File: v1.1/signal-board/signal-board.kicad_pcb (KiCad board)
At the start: 2 copper layers, 32 parts, among them SW1 SW_MEC_5G, SW2 SW_MEC_5G, U1 TPS63060, U2 ESP32-DEVKITC-32D

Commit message: footprint updates
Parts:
- added D1: Red LED, LED_THT:LED_D1.8mm_W3.3mm_H2.4mm, F.Cu at (256.4, 315.7)
- added D2: Green LED, LED_THT:LED_D1.8mm_W3.3mm_H2.4mm, F.Cu at (256.4, 321.4)
- added IC1: 74HCT245, 74HCT245:SOIC-20W_7.5x10.0mm_P1.27mm, F.Cu at (334.8, 248.2)
- added J1: Jack-DC, Connector_BarrelJack:BarrelJack_CUI_PJ-063AH_Horizontal, F.Cu at (322.4, 298.4)
- added J2: Conn_01x12, Connector_PinHeader_2.54mm:PinHeader_1x12_P2.54mm_Vertical, F.Cu at (300.8, 272.6)
- added J3: JST SM, jst-landing-pads:jst-smd-landing, F.Cu at (257.1, 296.4)
- added J4: Conn_01x16, Connector_PinHeader_2.54mm:PinHeader_1x16_P2.54mm_Vertical, F.Cu at (274.6, 335.6)
- SW1, SW2: footprint PTS525SM15SMTR2LFS:SW_PTS525SM15SMTR2LFS -> PTS 647:PTS647SK38SMTR2LFS
- moved U2 136.6 mm to (289.9, 297.4), turned to 90 degrees
- moved SW2 136.4 mm to (273.1, 272.9)
- moved L1 111.8 mm to (311.8, 248.0)
- moved U1 110.7 mm to (296.6, 247.2)
- moved R5 104.8 mm to (264.7, 245.3)
- moved C9 84.7 mm to (266.4, 205.4)
- moved R16 84.7 mm to (261.6, 205.4)
- moved C1 84.7 mm to (248.7, 222.8)
- moved C10 84.7 mm to (243.9, 226.8)
- moved C2 84.7 mm to (248.7, 219.8)
- moved C6 84.7 mm to (239.2, 229.8)
- moved C7 84.7 mm to (243.9, 223.9)
- moved R10 84.7 mm to (239.2, 218.0)
- moved R11 84.7 mm to (243.9, 218.0)
- moved R12 84.7 mm to (261.1, 210.6)
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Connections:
- net VDD renamed /3-12v
- C3 pad 1: Net-(C3-Pad1) -> /button_2
- C5 pad 1: Net-(C5-Pad1) -> /button_1
- C6 pad 1: /abc -> Net-(C6-Pad1)
- R10 pad 2: Net-(J2-Pad20) -> /pixels_1
- R11 pad 2: Net-(J2-Pad18) -> /pixels_2
- R12 pad 2: Net-(J2-Pad16) -> /pixels_3
- R13 pad 2: Net-(J2-Pad14) -> /pixels_4
- R14 pad 2: Net-(J2-Pad12) -> /pixels_5
- R15 pad 2: Net-(J2-Pad10) -> /pixels_6
- R16 pad 2: Net-(J2-Pad8) -> /pixels_7
- R17 pad 2: Net-(J2-Pad6) -> /pixels_8
- R2 pad 2: Net-(C3-Pad1) -> /button_2
- R3 pad 1: +5V -> +3V3
- R3 pad 2: Net-(C3-Pad1) -> /button_2
- R4 pad 2: Net-(C5-Pad1) -> /button_1
- R5 pad 1: Net-(R5-Pad1) -> Net-(D2-Pad1)
- R5 pad 2: Net-(D2-Pad1) -> GND
- R6 pad 1: +5V -> +3V3
- R6 pad 2: Net-(C5-Pad1) -> /button_1
- R7 pad 2: Net-(R7-Pad2) -> Net-(C6-Pad1)
- R8 pad 1: Net-(R7-Pad2) -> Net-(C6-Pad1)
- U1 pad 8: Net-(R7-Pad2) -> Net-(C6-Pad1)
- U2 pad 10: Net-(J2-Pad11) -> /level_shift_1
- U2 pad 11: Net-(J2-Pad13) -> /level_shift_2
- U2 pad 12: Net-(U2-Pad12) -> /status_led
- U2 pad 13: Net-(IC1-Pad7) -> /level_shift_3
- U2 pad 15: Net-(IC1-Pad8) -> /level_shift_4
- U2 pad 2: Net-(U2-Pad2) -> /en
- U2 pad 21: Net-(U2-Pad21) -> /vspi_mosi
- U2 pad 22: Net-(J2-Pad21) -> /i2c_scl
- U2 pad 23: Net-(J2-Pad19) -> /uart_tx
- U2 pad 24: Net-(J2-Pad17) -> /uart_rx
- U2 pad 25: Net-(J2-Pad15) -> /i2c_sda
- U2 pad 27: Net-(IC1-Pad3) -> /vspi_miso
- U2 pad 28: Net-(IC1-Pad4) -> /vspi_clk
- U2 pad 29: Net-(IC1-Pad5) -> /vspi_cs
- U2 pad 3: Net-(J2-Pad3) -> /sensor_vp
- U2 pad 30: Net-(IC1-Pad6) -> /level_shift_8
- U2 pad 31: Net-(U2-Pad31) -> /level_shift_7
- U2 pad 32: Net-(U2-Pad32) -> /level_shift_6
- U2 pad 33: Net-(U2-Pad33) -> /button_2
- U2 pad 34: Net-(U2-Pad34) -> /level_shift_5
- U2 pad 35: Net-(IC1-Pad9) -> /button_1
- U2 pad 4: Net-(J2-Pad5) -> /sensor_vn
- U2 pad 5: Net-(C5-Pad1) -> /io34
- U2 pad 6: Net-(C3-Pad1) -> /io35
- U2 pad 7: Net-(R5-Pad1) -> Net-(U2-Pad7)
- U2 pad 9: Net-(J2-Pad9) -> /io25
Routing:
- net /button_1: track 0.00 -> 4.48 mm
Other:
- board outline added: 88 x 64.7 mm
- board text added: "antenna"
- board text added: "button"
- board text added: "indicators"
- board text added: "pins"
- board text added: "pixels"
- board text added: "power"

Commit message: layout
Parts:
- added J5: switch_jumpers, Connector_PinHeader_2.54mm:PinHeader_1x02_P2.54mm_Vertical, B.Cu at (106.7, 124.5)
- added J6: switch_jumpers, Connector_PinHeader_2.54mm:PinHeader_1x02_P2.54mm_Vertical, B.Cu at (106.7, 119.4)
- C1, C2, D1, D2, IC1, L1, R10, R11, R12, R13, R14, R15, R16, R17, R4, U1: moved to B.Cu
- C10: renamed from C8; moved to B.Cu
- C3: renamed from C4; moved to B.Cu
- C4: renamed from C6; moved to B.Cu
- C5: renamed from C7; moved to B.Cu
- C6: renamed from C9; moved to B.Cu
- C7: renamed from C10; moved to B.Cu
- C8: renamed from C5; moved to B.Cu
- C9: renamed from C3; moved to B.Cu
- R1: renamed from R7; moved to B.Cu
- R2: renamed from R8; moved to B.Cu
- R3: renamed from R9; moved to B.Cu
- R5: renamed from R6; moved to B.Cu
- R6: renamed from R2; moved to B.Cu
- R7: renamed from R3; moved to B.Cu
- R8: renamed from R1; moved to B.Cu
- R9: renamed from R5; moved to B.Cu
- SW1: renamed from SW2; moved to B.Cu
- SW2: renamed from SW1; moved to B.Cu
- moved J4 258.3 mm to (109.2, 137.2)
- moved D2 255.0 mm to (112.3, 111.0)
- moved J2 253.0 mm to (114.3, 101.6)
- moved D1 252.6 mm to (108.5, 111.0), turned to 180 degrees
- moved J1 250.2 mm to (156.8, 110.9)
- moved U2 242.1 mm to (125.7, 119.4)
- moved IC1 239.9 mm to (130.8, 121.9), turned to 90 degrees
- moved SW1 217.7 mm to (112.5, 125.9), turned to 180 degrees
- moved SW2 211.2 mm to (112.5, 120.7), turned to 180 degrees
- moved L1 209.9 mm to (151.6, 112.4), turned to 180 degrees
- moved R9 200.0 mm to (113.5, 114.3)
- moved J3 195.3 mm to (158.2, 128.0), turned to 180 degrees
- moved U1 194.6 mm to (151.8, 117.1), turned to 180 degrees
- moved R15 184.8 mm to (125.2, 110.8), turned to 90 degrees
- moved R17 184.6 mm to (120.7, 110.7), turned to 90 degrees
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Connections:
- J2 pad 1: GND -> /i2c_scl
- J2 pad 10: GND -> /pixels_2
- J2 pad 11: +5V -> /pixels_1
- J2 pad 12: /en -> GND
- J2 pad 2: /pixels_1 -> /i2c_sda
- J2 pad 3: /pixels_2 -> GND
- J2 pad 4: /pixels_3 -> /pixels_8
- J2 pad 5: /pixels_4 -> /pixels_7
- J2 pad 6: /pixels_5 -> /pixels_6
- J2 pad 7: /pixels_6 -> /pixels_5
- J2 pad 8: /pixels_7 -> /pixels_4
- J2 pad 9: /pixels_8 -> /pixels_3
- J4 pad 10: /uart_tx -> /vspi_mosi
- J4 pad 11: /uart_rx -> /vspi_miso
- J4 pad 12: /vspi_mosi -> /vspi_clk
- J4 pad 13: /vspi_miso -> /vspi_cs
- J4 pad 14: /vspi_clk -> GND
- J4 pad 15: /vspi_cs -> +5V
- J4 pad 2: GND -> /en
- J4 pad 3: /i2c_sda -> /sensor_vp
- J4 pad 4: /i2c_scl -> /sensor_vn
- J4 pad 5: /sensor_vp -> /io34
- J4 pad 6: /sensor_vn -> /io35
- J4 pad 7: /io34 -> /io25
- J4 pad 8: /io35 -> /uart_tx
- J4 pad 9: /io25 -> /uart_rx
- U2 pad 10: /level_shift_1 -> /level_shift_4
- U2 pad 11: /level_shift_2 -> /level_shift_3
- U2 pad 13: /level_shift_3 -> /level_shift_2
- U2 pad 15: /level_shift_4 -> /level_shift_1
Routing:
- net /3-12v: track 0.00 -> 127.5 mm
- net +5V: track 0.00 -> 61.5 mm
- net +3V3: track 0.00 -> 53.7 mm, vias 0 -> 2
- net /vspi_mosi: track 0.00 -> 48.3 mm
- net /pixels_2: track 0.00 -> 46.3 mm, vias 0 -> 2
- net /pixels_1: track 0.00 -> 44.7 mm, vias 0 -> 2
- net /uart_tx: track 0.00 -> 39.4 mm
- net /vspi_cs: track 0.00 -> 37.3 mm
- net /vspi_clk: track 0.00 -> 37.1 mm
- net /vspi_miso: track 0.00 -> 37.0 mm
- net /uart_rx: track 0.00 -> 36.0 mm
- net /status_led: track 0.00 -> 29.4 mm
- net /button_1: track 4.48 -> 33.7 mm, vias 0 -> 1
- net /button_2: track 0.00 -> 27.5 mm, vias 0 -> 1
- net /level_shift_5: track 0.00 -> 23.7 mm, vias 0 -> 1
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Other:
- board size 88 x 64.7 mm -> 71 x 42 mm
- copper layers 2 -> 4
- net class Default: clearance 0.254 -> 0.2
- rule trace_clearance: 0.254 -> 0.2
- board text added: "You're looking at the back. Buttons / LEDs"
- board text added: "You're looking at the back. Pins / LED strip / DC Jack / ESP32"
- board text removed: "antenna"
- board text removed: "button"
- board text removed: "indicators"
- board text removed: "pins"
- board text removed: "pixels"
- board text removed: "power"

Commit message: JLC PCB changes
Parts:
- C8, C9: footprint Capacitor_SMD:C_0805_2012Metric_Pad1.15x1.40mm_HandSolder -> Capacitor_SMD:C_0402_1005Metric
- R4, R5, R6, R7: footprint Resistor_SMD:R_0805_2012Metric_Pad1.15x1.40mm_HandSolder -> Resistor_SMD:R_0402_1005Metric
- R8, R9: value 660 -> 680; footprint Resistor_SMD:R_0805_2012Metric_Pad1.15x1.40mm_HandSolder -> Resistor_SMD:R_0402_1005Metric
- turned C8 to 90 degrees
- turned C9 to 90 degrees
- turned R4 to -90 degrees
- turned R5 to -90 degrees
- turned R6 to -90 degrees
- turned R7 to -90 degrees
- turned R9 to 180 degrees
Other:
- board text added: "You're looking at the front. Pins / LED strip / DC Jack / ESP32"
- board text removed: "You're looking at the back. Pins / LED strip / DC Jack / ESP32"

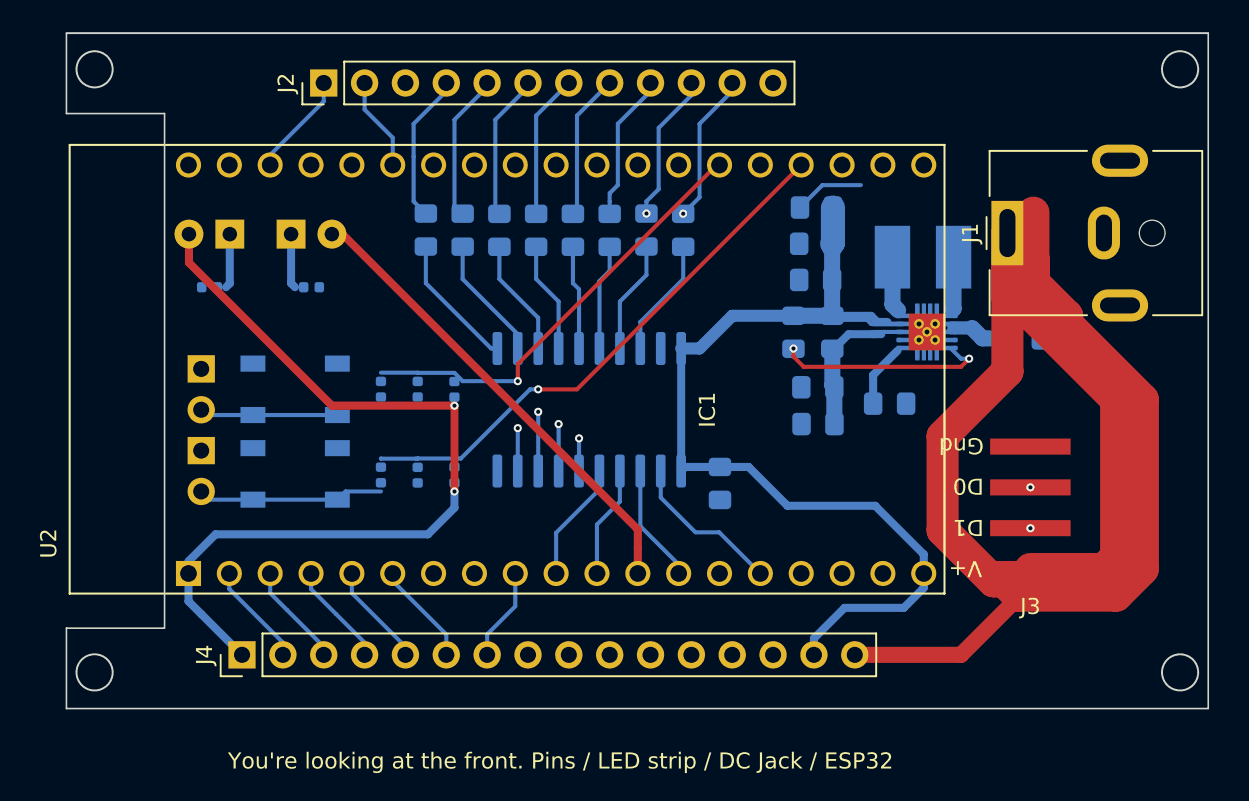
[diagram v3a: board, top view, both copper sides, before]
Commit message: updated v1.1 power layout
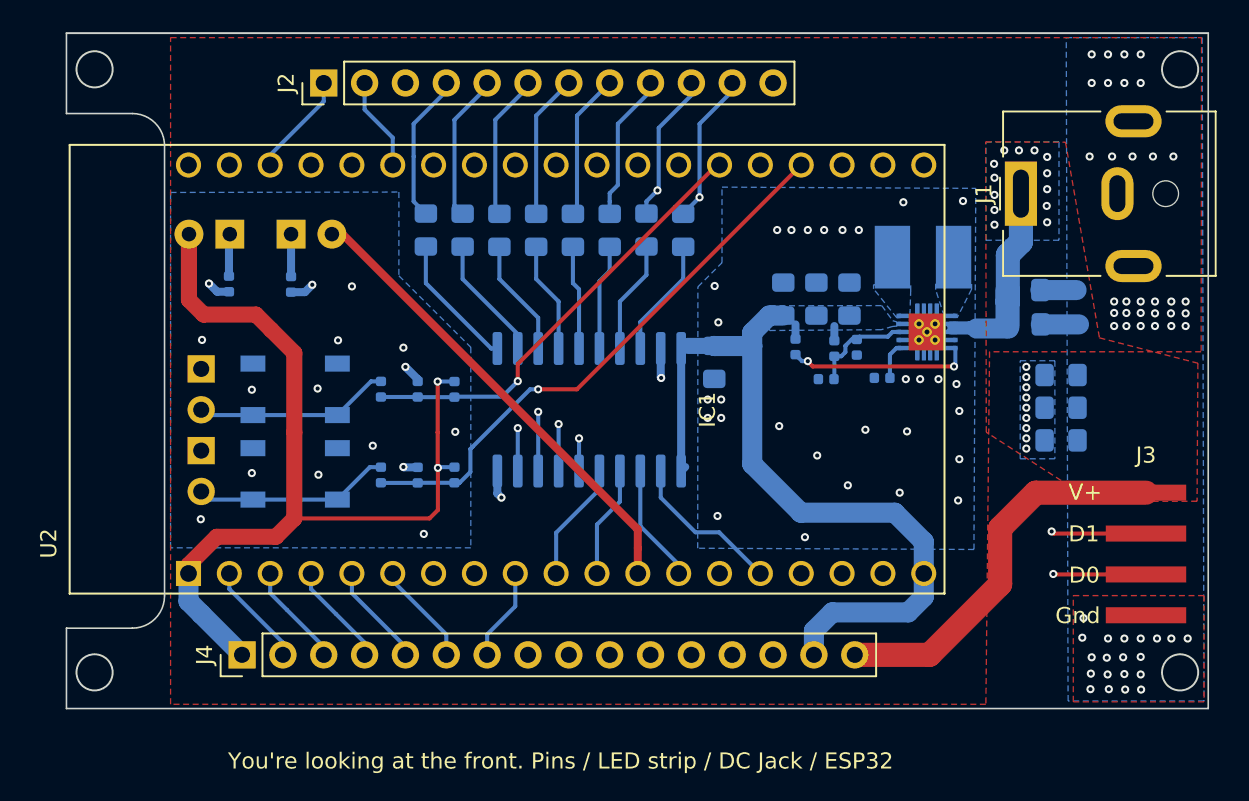
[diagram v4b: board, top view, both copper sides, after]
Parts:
- added C11: 10uF, Capacitor_SMD:C_0805_2012Metric_Pad1.15x1.40mm_HandSolder, B.Cu at (160.1, 119.8)
- added C12: 10uF, Capacitor_SMD:C_0805_2012Metric_Pad1.15x1.40mm_HandSolder, B.Cu at (160.1, 121.8)
- added C13: 10uF, Capacitor_SMD:C_0805_2012Metric_Pad1.15x1.40mm_HandSolder, B.Cu at (160.1, 123.8)
- C3, C4: footprint Capacitor_SMD:C_0805_2012Metric_Pad1.15x1.40mm_HandSolder -> Capacitor_SMD:C_0402_1005Metric
- R1, R2, R3: footprint Resistor_SMD:R_0805_2012Metric_Pad1.15x1.40mm_HandSolder -> Resistor_SMD:R_0402_1005Metric
- moved J3 7.74 mm to (165.4, 130.9), turned to 0 degrees
- moved C10 7.54 mm to (138.6, 119.0)
- moved C5 6.05 mm to (142.9, 115.0), turned to 90 degrees
- moved R2 5.35 mm to (147.4, 118.0), turned to -90 degrees
- moved C6 3.44 mm to (144.9, 115.0), turned to 90 degrees
- moved J1 2.59 mm to (157.7, 108.5)
- moved C7 2.41 mm to (147.0, 115.0), turned to 90 degrees
- moved C3 1.67 mm to (149.0, 119.9), turned to 180 degrees
- moved R9 1.28 mm to (112.3, 114.1), turned to -90 degrees
- moved R8 1.23 mm to (108.4, 114.1), turned to -90 degrees
- moved R1 1.01 mm to (146.1, 118.1)
- moved R3 0.91 mm to (143.6, 118.0)
- moved C2 0.87 mm to (157.9, 116.6)
- moved C1 0.75 mm to (157.8, 114.5)
- moved C4 0.72 mm to (145.5, 120.0)
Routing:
- net /3-12v: track 127.5 -> 38.8 mm, vias 0 -> 23
- net GND: track 4.74 -> 18.4 mm, vias 0 -> 97
- net +5V: track 61.5 -> 49.7 mm
- net /pixels_2: track 46.3 -> 55.9 mm
- net /pixels_1: track 44.7 -> 52.3 mm
- net +3V3: track 53.7 -> 58.3 mm
- net Net-(C4-Pad1): track 10.4 -> 6.31 mm
- net /L1PB: track 4.22 -> 0.77 mm
- net /L1PA: track 3.28 -> 0.00 mm
- net Net-(R3-Pad2): track 13.3 -> 11.4 mm
- net Net-(C3-Pad1): track 3.93 -> 2.45 mm
- net /button_1: track 33.7 -> 35.2 mm
- net Net-(D1-Pad1): track 3.40 -> 2.63 mm
- net Net-(D2-Pad1): track 3.40 -> 2.64 mm
- net Net-(J5-Pad2): track 11.6 -> 12.2 mm
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- added copper zone on B.Cu, net +5V
- added copper zone on B.Cu, net /3-12v
- added copper zone on F.Cu, net /3-12v
- added copper zone on B.Cu, net /L1PA
- added copper zone on B.Cu, net /L1PB
- added copper zone on B.Cu, net GND
- added copper zone on F.Cu, net GND
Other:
- outline, holes or cut-outs redrawn

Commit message: updated notes and updates from board review
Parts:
- added G***: LOGO, WiFi LED Logo:wifi_to_led_18mm, B.Cu at (157.1, 131.2)
- added G***: LOGO, WiFi LED Logo:wifi_to_led_18mm, F.Cu at (156.0, 131.2)
- added TP1: TestPoint, TestPoint:TestPoint_Pad_D1.0mm, B.Cu at (154.2, 119.6)
- R4, R6: value 1k -> 1K
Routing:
- net Net-(R3-Pad2): track 11.4 -> 12.3 mm
- net GND: vias 97 -> 114

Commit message: circuit updates
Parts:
- moved J1 2.00 mm to (159.7, 108.5)
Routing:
- net /3-12v: track 38.8 -> 37.0 mm
- net GND: vias 114 -> 113
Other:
- board size 71 x 42 mm -> 73 x 43 mm
- board text added: "25"
- board text added: "3-12v"
- board text added: "3.3V"
- board text added: "34"
- board text added: "35"
- board text added: "5v"
- board text added: "P1"
- board text added: "P2"
- board text added: "P3"
- board text added: "P4"
- board text added: "P5"
- board text added: "P6"
- board text added: "P7"
- board text added: "P8"
- board text added: "RX"
- board text added: "TX"
- board text added: "You're looking at the front. Pins / LED strip / DC Jack / ESP32 Box bottom walls are 74.82mm long by 45.19mm wide"
- board text added: "clk"
- board text added: "cs"
- board text added: "en"
- board text added: "gnd"
- board text added: "miso"
- board text added: "mosi"
- board text added: "scl"
- board text added: "sda"
- board text added: "vn"
- board text added: "vp"
- board text removed: "You're looking at the front. Pins / LED strip / DC Jack / ESP32"
